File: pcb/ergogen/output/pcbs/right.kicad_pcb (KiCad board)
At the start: 2 copper layers, 143.4 x 86.2 mm, 49 parts

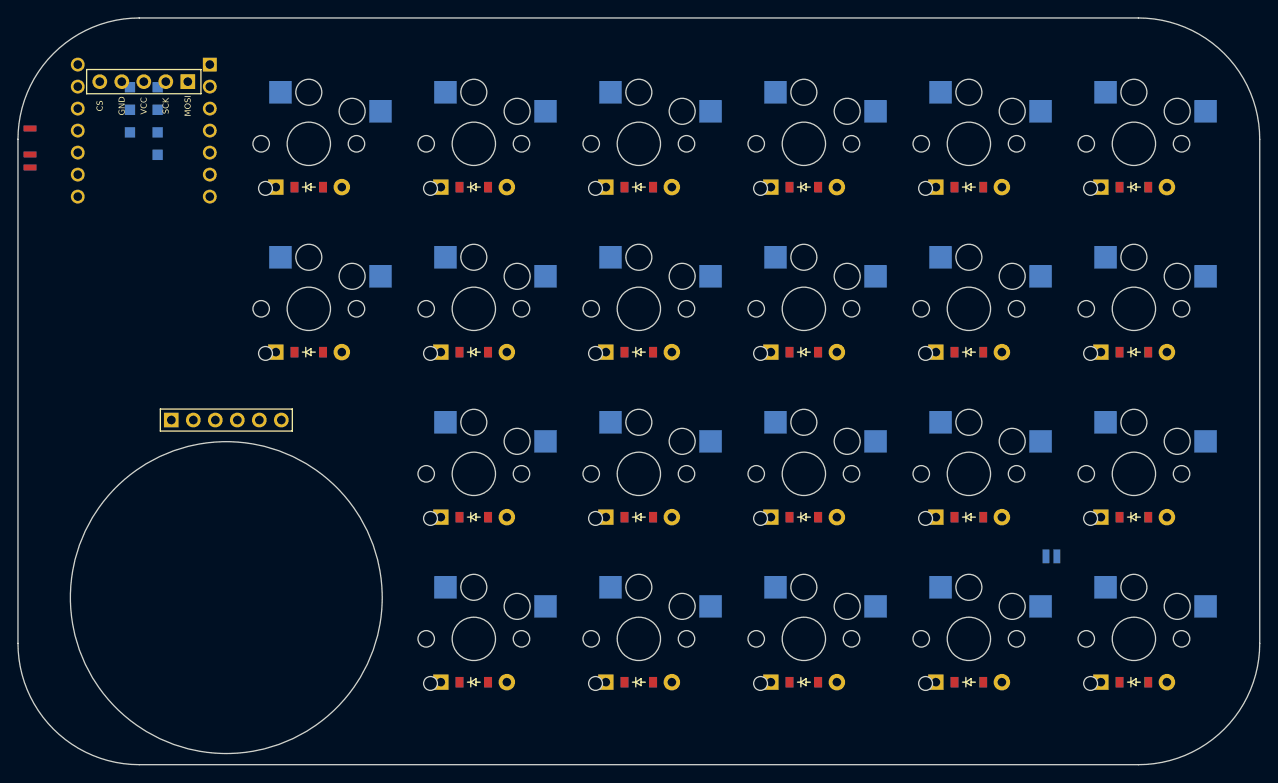
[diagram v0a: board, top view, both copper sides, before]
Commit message: Gasket-mount PCB/plate outlines and 3D-printable case
- Ergogen: cavity/top-opening outlines, plate with 6 gasket tabs,
  PCB 0.75mm inside the case with tongues for USB-C and power switch
- XIAO turned sideways so USB-C exits the inner side wall
- case/kataware_case.py builds top and bottom case STLs from the DXFs
- Section drawings, 3D renders and README/KiCad guide updates

Co-Authored-By: Claude Opus 5.5 <noreply@anthropic.com>
Claude-Session: https://claude.ai/code/session_017zNm7dMSTHELcztuNr6aNy
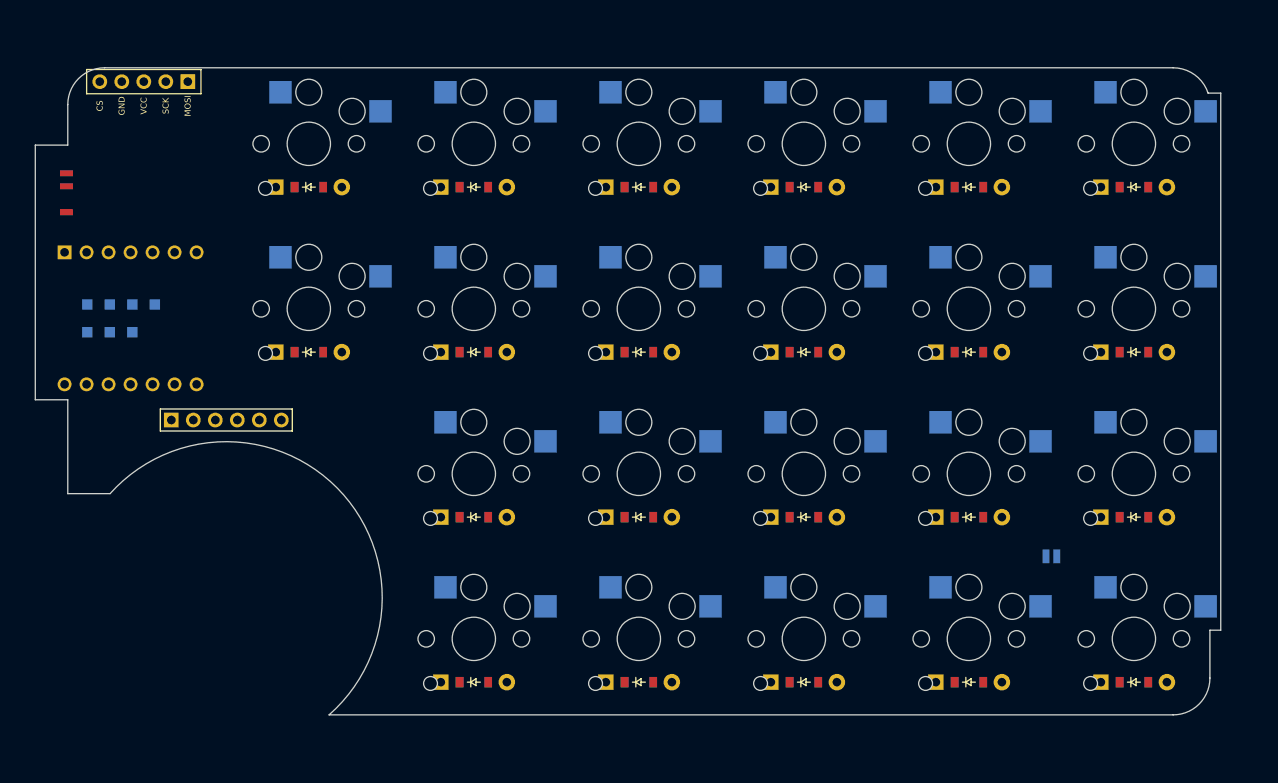
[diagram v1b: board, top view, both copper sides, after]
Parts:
- moved MCU1 21.7 mm to (198.5, -37.0), turned to 90 degrees
- moved PWR1 5.17 mm to (189.0, -51.5), turned to 90 degrees
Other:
- board size 143.4 x 86.2 mm -> 136.9 x 74.7 mm

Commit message: Move the trackball under the [ ] column at the N row
- Ball centre to (-8, 11) from the e column / thumb row: the cover now
  ends ~1mm below the ] keycap and ~1mm from N/Enter (the limit)
- The unit now sits inside the case cavity, so the right case wall
  bulge is gone and both halves share the same cavity
- XIAO raised 1.5mm to clear the ball hole; sensor cable moves to a
  JST SH 6-pin SMD connector (J) on the back between Enter and N, and
  the base cable exit faces it
- Fix draw_case_section so the thumb/tab/USB sections are written again
- README, KiCad guide, template and images updated

Co-Authored-By: Claude Opus 5.5 <noreply@anthropic.com>
Claude-Session: https://claude.ai/code/session_017zNm7dMSTHELcztuNr6aNy
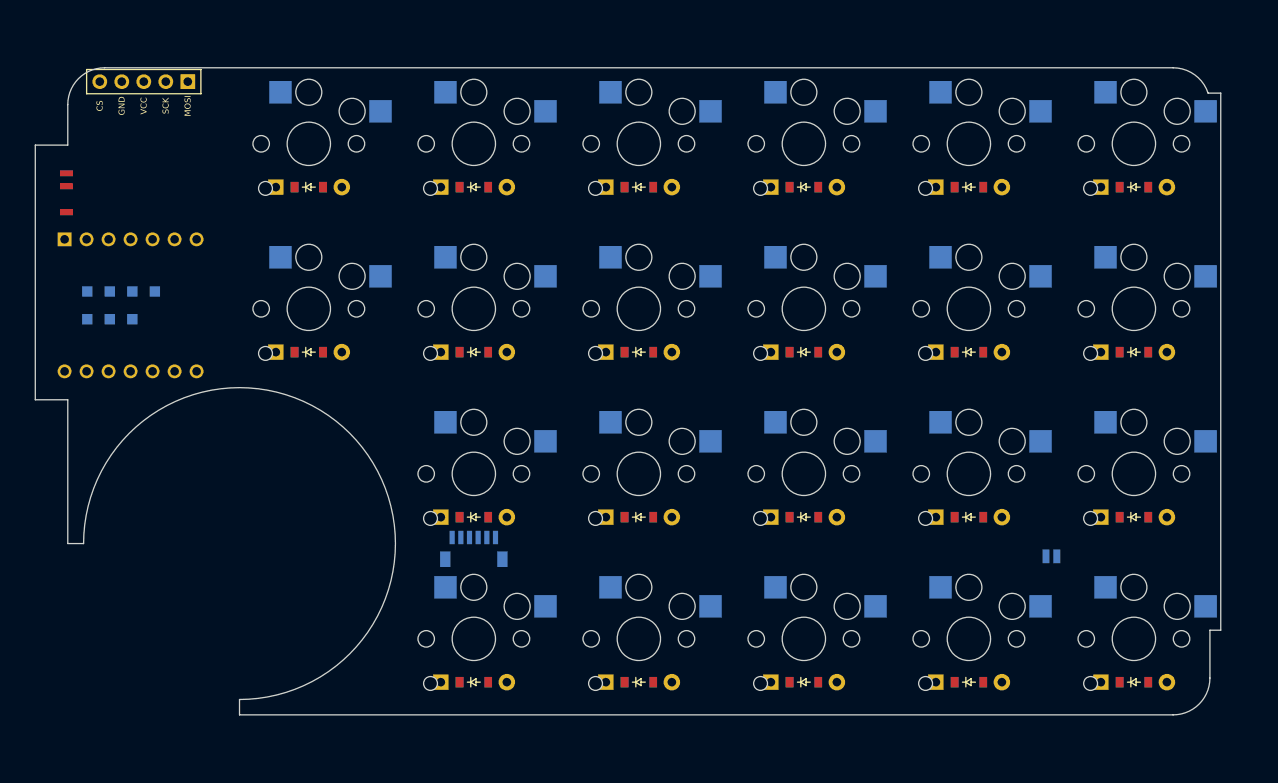
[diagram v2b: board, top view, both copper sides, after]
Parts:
- J1: footprint header6 -> kataware_jst_sh6_placeholder; moved to B.Cu
- moved J1 32.2 mm to (238.1, -10.4)
- moved MCU1 1.50 mm to (198.5, -38.5)
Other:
- outline, holes or cut-outs redrawn
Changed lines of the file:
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@@
   (title_block
     (title "right")
-    (date "2026-10-16")
+    (date "2026-10-17")
     (rev "0.1")
     (company "kyonccc")
@@
         (pad 2 thru_hole circle (at 3.81 0 0) (size 1.905 1.905) (drill 0.9906) (layers *.Cu *.Mask) (net 28 "right_c12_top"))
     )
-      (module header6 (layer F.Cu)
-      (at 209.525 -25.262500000000006 0)
-      (fp_text reference "J1" (at 0 -2) (layer F.SilkS) hide (effects (font (size 1 1) (thickness 0.15))))
-      (fp_text value "" (at 0 0) (layer F.SilkS) hide (effects (font (size 1 1) (thickness 0.15))))
-      (fp_line (start -7.62 -1.27) (end 7.62 -1.27) (layer F.SilkS) (width 0.15))
-      (fp_line (start 7.62 -1.27) (end 7.62 1.27) (layer F.SilkS) (width 0.15))
-      (fp_line (start 7.62 1.27) (end -7.62 1.27) (layer F.SilkS) (width 0.15))
-      (fp_line (start -7.62 1.27) (end -7.62 -1.27) (layer F.SilkS) (width 0.15))
-      (pad 1 thru_hole rect (at -6.35 0) (size 1.7 1.7) (drill 1.0) (layers *.Cu *.Mask) (net 33 "3V3"))
-(pad 2 thru_hole circle (at -3.81 0) (size 1.7 1.7) (drill 1.0) (layers *.Cu *.Mask) (net 34 "GND"))
-(pad 3 thru_hole circle (at -1.27 0) (size 1.7 1.7) (drill 1.0) (layers *.Cu *.Mask) (net 35 "TB_SCLK"))
-(pad 4 thru_hole circle (at 1.27 0) (size 1.7 1.7) (drill 1.0) (layers *.Cu *.Mask) (net 36 "TB_SDIO"))
-(pad 5 thru_hole circle (at 3.81 0) (size 1.7 1.7) (drill 1.0) (layers *.Cu *.Mask) (net 37 "TB_NCS"))
-(pad 6 thru_hole circle (at 6.35 0) (size 1.7 1.7) (drill 1.0) (layers *.Cu *.Mask) (net 38 "TB_MOTION"))
+      (module kataware_jst_sh6_placeholder (layer B.Cu)
+      (at 238.10000000000002 -10.400000000000006 0)
+      (fp_text reference "J1" (at 0 3.2) (layer B.SilkS) hide (effects (font (size 1 1) (thickness 0.15)) (justify mirror)))
+      (fp_text value "" (at 0 0) (layer B.SilkS) hide (effects (font (size 1 1) (thickness 0.15))))
+      (fp_text user "J (仮) JST SH 6P" (at 0 0 0) (layer B.Fab) (effects (font (size 0.6 0.6) (thickness 0.1)) (justify mirror)))
+      (fp_line (start -4 -2.2) (end 4 -2.2) (layer B.Fab) (width 0.1))
+      (fp_line (start 4 -2.2) (end 4 2.2) (layer B.Fab) (width 0.1))
+      (fp_line (start 4 2.2) (end -4 2.2) (layer B.Fab) (width 0.1))
+      (fp_line (start -4 2.2) (end -4 -2.2) (layer B.Fab) (width 0.1))
+      (pad 1 smd rect (at -2.50 -1.3 0) (size 0.6 1.55) (layers B.Cu B.Paste B.Mask) (net 33 "3V3"))
+(pad 2 smd rect (at -1.50 -1.3 0) (size 0.6 1.55) (layers B.Cu B.Paste B.Mask) (net 34 "GND"))
+(pad 3 smd rect (at -0.50 -1.3 0) (size 0.6 1.55) (layers B.Cu B.Paste B.Mask) (net 35 "TB_SCLK"))
+(pad 4 smd rect (at 0.50 -1.3 0) (size 0.6 1.55) (layers B.Cu B.Paste B.Mask) (net 36 "TB_SDIO"))
+(pad 5 smd rect (at 1.50 -1.3 0) (size 0.6 1.55) (layers B.Cu B.Paste B.Mask) (net 37 "TB_NCS"))
+(pad 6 smd rect (at 2.50 -1.3 0) (size 0.6 1.55) (layers B.Cu B.Paste B.Mask) (net 38 "TB_MOTION"))
+      (pad "" smd rect (at -3.3 1.2 0) (size 1.2 1.8) (layers B.Cu B.Paste B.Mask))
+      (pad "" smd rect (at 3.3 1.2 0) (size 1.2 1.8) (layers B.Cu B.Paste B.Mask))
       )
       (module kataware_xiao_plus_placeholder (layer B.Cu)
-      (at 198.47500000000002 -37.00000000000001 90)
+      (at 198.47500000000002 -38.50000000000001 90)
       (fp_text reference "MCU1" (at 0 -12) (layer B.SilkS) hide (effects (font (size 1 1) (thickness 0.15)) (justify mirror)))
       (fp_text value "" (at 0 0) (layer B.SilkS) hide (effects (font (size 1 1) (thickness 0.15)) (justify mirror)))
@@
     (pad 2 smd rect (at 0.625 0 0) (size 0.8 1.6) (layers B.Cu B.Paste B.Mask) (net 43 "BAT_P"))
     )
-  (gr_line (start 221.3882244 8.774999999999997) (end 318.82500000000005 8.774999999999995) (layer Edge.Cuts) (stroke (width 0.15) (type default)))
+  (gr_line (start 211.05 8.774999999999995) (end 318.82500000000005 8.774999999999995) (layer Edge.Cuts) (stroke (width 0.15) (type default)))
 (gr_arc (start 318.82500000000005 8.774999999999995) (mid 321.83020380000005 7.530203799999995) (end 323.07500000000005 4.524999999999995) (layer Edge.Cuts) (stroke (width 0.15) (type default)))
 (gr_line (start 323.07500000000005 4.524999999999995) (end 323.07500000000005 -1.000000000000007) (layer Edge.Cuts) (stroke (width 0.15) (type default)))
@@
 (gr_arc (start 195.47500000000002 -65.92500000000001) (mid 192.46979620000002 -64.68020380000002) (end 191.22500000000002 -61.67500000000001) (layer Edge.Cuts) (stroke (width 0.15) (type default)))
 (gr_line (start 191.22500000000002 -61.67500000000001) (end 191.22500000000002 -57) (layer Edge.Cuts) (stroke (width 0.15) (type default)))
-(gr_line (start 191.22500000000002 -27.600000000000005) (end 191.22500000000002 -16.762500000000003) (layer Edge.Cuts) (stroke (width 0.15) (type default)))
+(gr_line (start 191.22500000000002 -27.600000000000005) (end 191.22500000000002 -11.000000000000007) (layer Edge.Cuts) (stroke (width 0.15) (type default)))
 (gr_line (start 323.07500000000005 -1.000000000000007) (end 324.32500000000005 -1.000000000000007) (layer Edge.Cuts) (stroke (width 0.15) (type default)))
 (gr_line (start 324.32500000000005 -1.000000000000007) (end 324.32500000000005 -63.00000000000001) (layer Edge.Cuts) (stroke (width 0.15) (type default)))
@@
 (gr_line (start 191.22500000000002 -57) (end 187.47500000000002 -57) (layer Edge.Cuts) (stroke (width 0.15) (type default)))
 (gr_line (start 187.47500000000002 -57) (end 187.47500000000002 -27.600000000000005) (layer Edge.Cuts) (stroke (width 0.15) (type default)))
-(gr_arc (start 221.3882244 8.774999999999997) (mid 222.3173442 -17.425672100000003) (end 196.1085921 -16.762500000000003) (layer Edge.Cuts) (stroke (width 0.15) (type default)))
-(gr_line (start 196.1085921 -16.7625) (end 191.22500000000002 -16.762500000000003) (layer Edge.Cuts) (stroke (width 0.15) (type default)))
+(gr_arc (start 211.05 6.999999999999993) (mid 223.7779221 -23.727922100000008) (end 193.05 -11.000000000000007) (layer Edge.Cuts) (stroke (width 0.15) (type default)))
+(gr_line (start 211.05 8.774999999999995) (end 211.05 6.999999999999993) (layer Edge.Cuts) (stroke (width 0.15) (type default)))
+(gr_line (start 193.05 -11.000000000000007) (end 191.22500000000002 -11.000000000000007) (layer Edge.Cuts) (stroke (width 0.15) (type default)))
 )
